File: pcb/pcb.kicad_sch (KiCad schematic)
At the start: 35 parts, among them J1 Screw Connector, J10 Conn_02x10_Counter_Clockwise, J11 Conn_01x10, J2 Screw Connector, J3 Screw Connector, J4 Screw Connector, J5 Conn_01x03, J6 Conn_01x03, J7 Conn_01x03, J8 Conn_01x03, J9 Conn_01x03, Q1 IRF9Z34NPBF, Q2 IRF9Z34NPBF, Q3 IRF9Z34NPBF, Q4 IRF9Z34NPBF, Q5 IRF9Z34NPBF, U1 ACS711ELCTR-12AB-T, U2 ACS711ELCTR-12AB-T, U3 ACS711ELCTR-12AB-T, U4 ACS711ELCTR-12AB-T, U5 ACS711ELCTR-12AB-T, U6 TXS0102DCUR, U7 TXS0102DCUR, U8 TXS0102DCUR

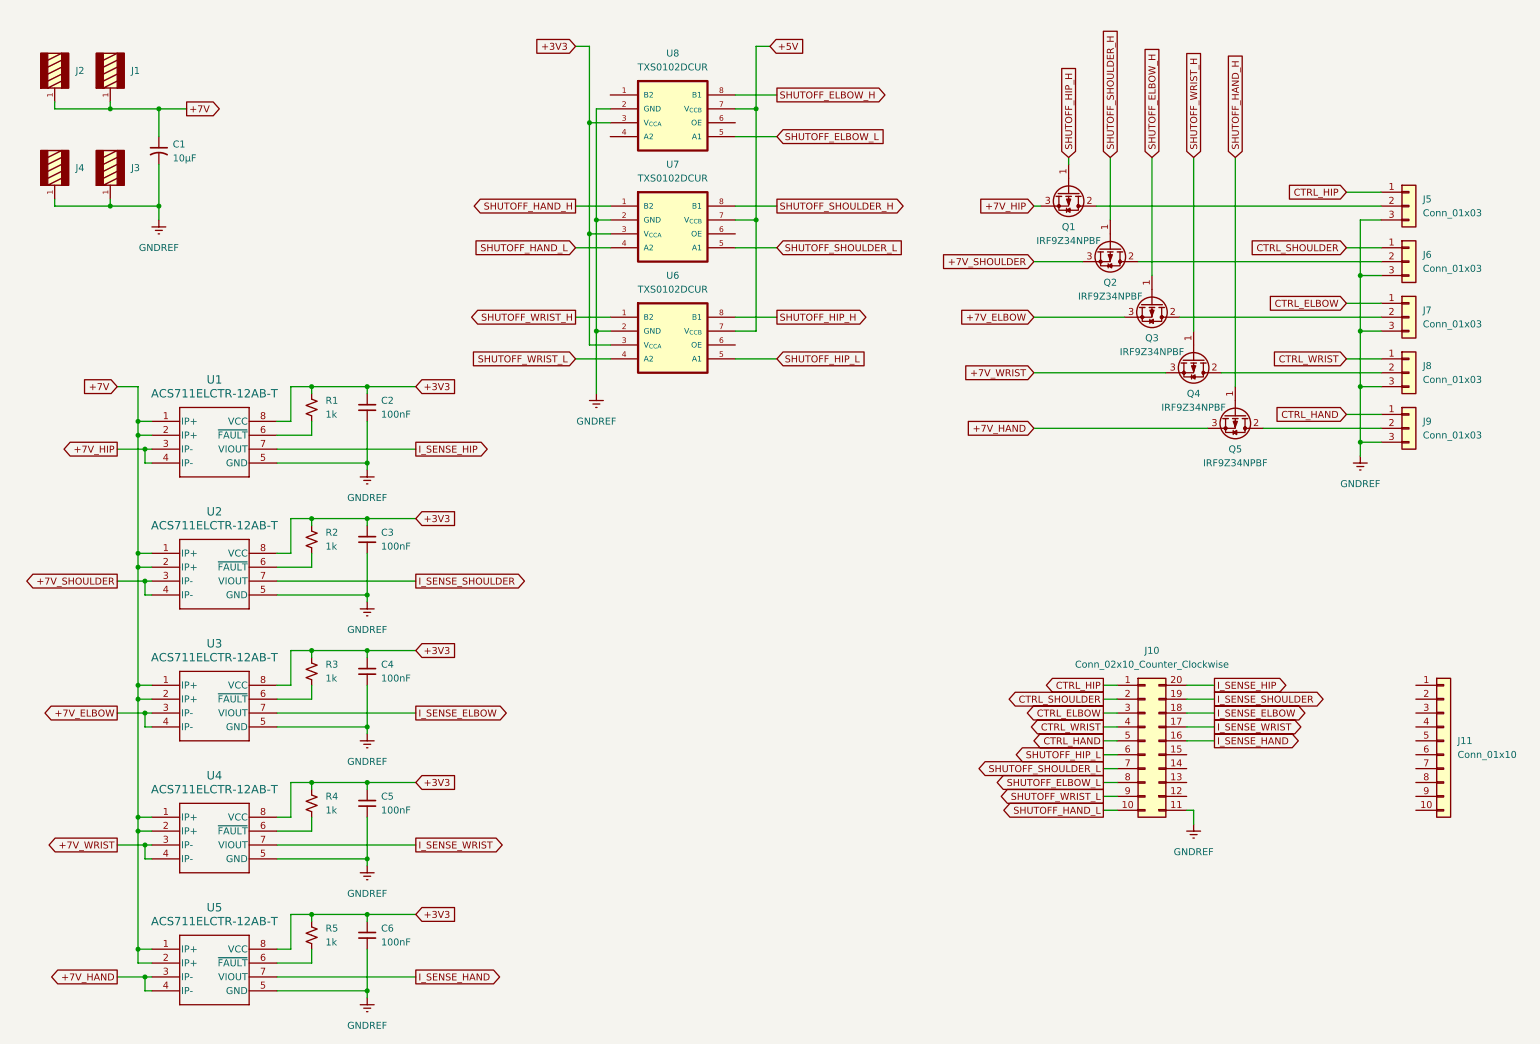
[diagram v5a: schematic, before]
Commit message: Add 5V LDO regulator to schematic
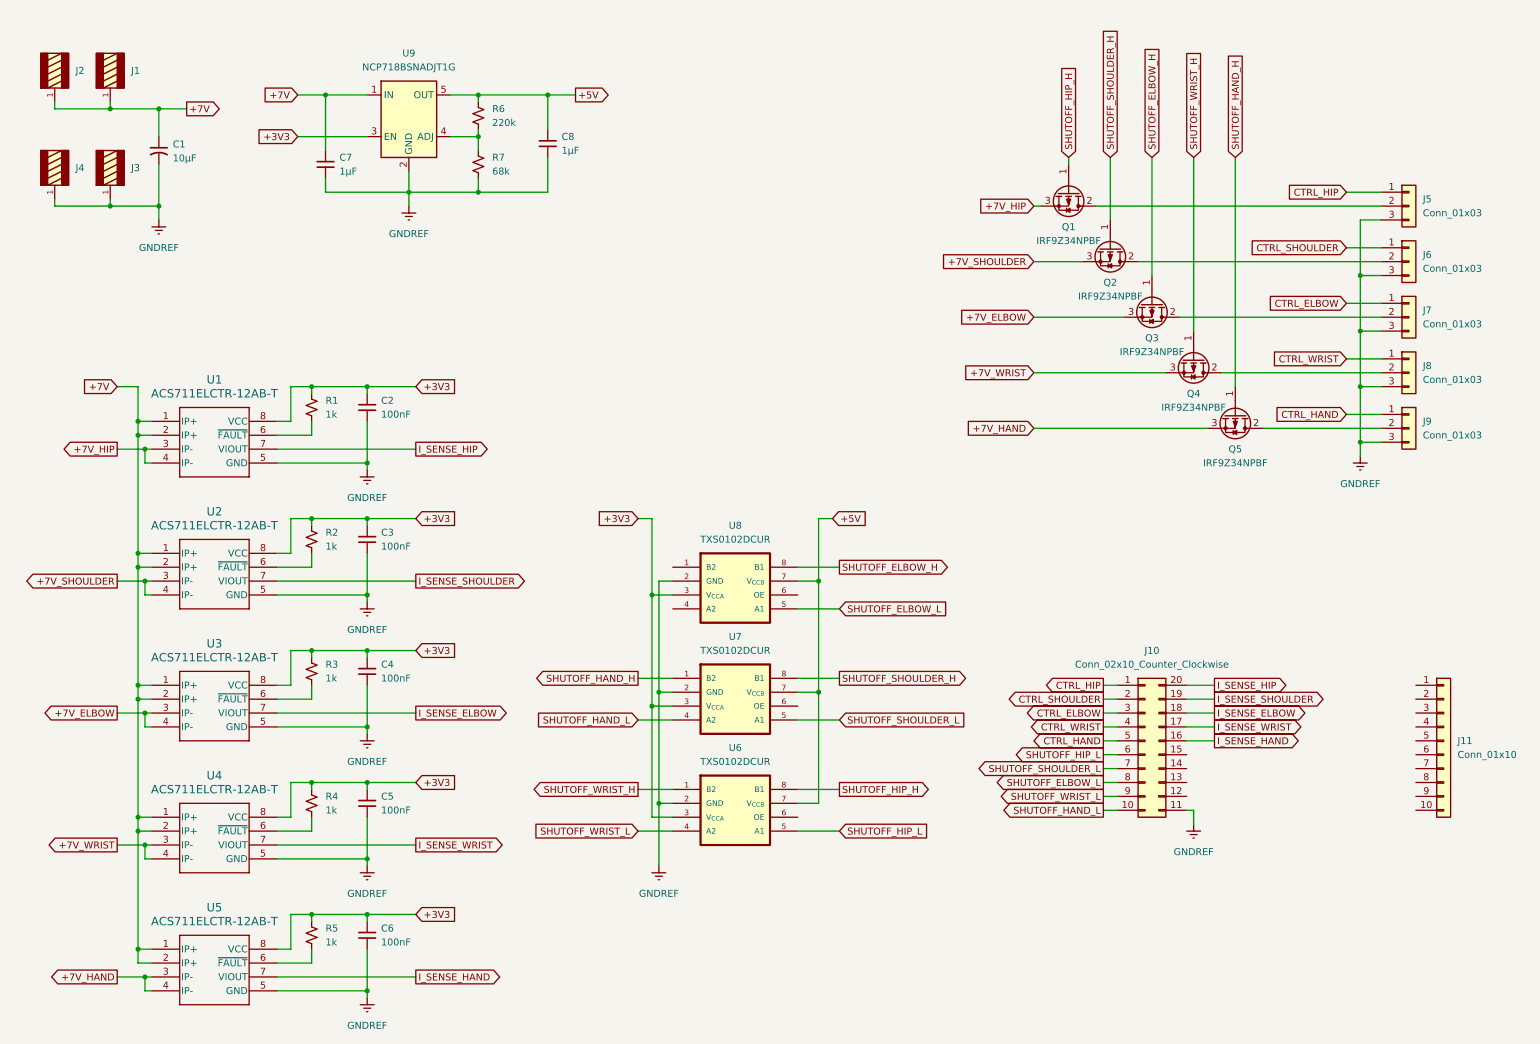
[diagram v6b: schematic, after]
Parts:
- added C7, C8: 1µF, symbol Device:C_Small
- added R6: 220k, symbol Device:R_Small_US
- added R7: 68k, symbol Device:R_Small_US
- added U9: NCP718BSNADJT1G, symbol lib:NCP718BSNADJT1G
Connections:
- net +3V3: now also U9.3 (EN)
- net +5V: now also C8.1, R6.1, U9.5 (OUT)
- net +7V: now also C7.1, U9.1 (IN)
- net GNDREF: now also C7.2, C8.2, R7.2, U9.2 (GND)
- new net: R6.2, R7.1, U9.4 (ADJ)
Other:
- moved on the sheet: U6, U7, U8
